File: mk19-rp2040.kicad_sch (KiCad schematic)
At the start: 134 parts, among them J1 USB_C_Receptacle_USB2.0, J10 Conn_01x02, J11 Conn_01x03_Socket, J12 USB_C_Receptacle_USB2.0, J13 USB_C_Receptacle_USB2.0, J2 Conn_01x03_Socket, J3 Conn_01x02_Socket, J4 Conn_01x06_Socket, J5 Conn_01x02, J7 Conn_01x02_Socket, J8 Conn_01x02_Socket, J9 Conn_01x02_Socket, T1 Conn_01x01_Socket, T10 Conn_01x01_Socket, T11 Conn_01x01_Socket, T12 Conn_01x01_Socket, T13 Conn_01x01_Socket, T14 Conn_01x01_Socket, T15 Conn_01x01_Socket, T2 Conn_01x01_Socket, T3 Conn_01x01_Socket, T5 Conn_01x01_Socket, T6 Conn_01x01_Socket, T7 Conn_01x01_Socket, T9 Conn_01x01_Socket, U1 RP2040, U10 1N4148W_C81598, U11 1N4148W_C81598, U12 1N4148W_C81598, U13 1N4148W_C81598, U14 1N4148W_C81598, U15 1N4148W_C81598, U2 USBLC6-2P6, U3 XC6210B332MR-G, U4 USBLC6-2P6, U5 W25Q128JVS, U6 8_01A0_008200, U7 8_01A0_008200, U8 USBLC6-2P6, U9 1N4148W_C81598, Y1 Crystal_GND24

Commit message: more changes, pcba insights coming next
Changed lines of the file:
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@@
-		)
-	)
-	(text_box "todo: Burkfers suggests 5v over serial is incorrect.\nreview how chunky does it."
-		(exclude_from_sim no)
-		(at 582.93 289.56 0)
-		(size 40.64 8.89)
-		(stroke
-			(width 0)
-			(type default)
-		)
-		(fill
-			(type none)
-		)
-		(effects
-			(font
-				(face "Futura")
-				(size 1.27 1.27)
-			)
-			(justify left top)
 		)
 	)

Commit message: reworking some of this, copy paste introduced errors whee
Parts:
- removed C20, C21, C22: CL31B105KBHNNNE, ct-kicad:C1206, symbol ct-kicad:CL31B105KBHNNNE
- removed U5: W25Q128JVS, drawings:W25Q128JVPIQ, symbol Memory_Flash:W25Q128JVS
- added C2, C28, C29: 10u, ct-kicad:C0805, symbol Device:C
- added FID1, FID2, FID3, FID4: Fiducial, Fiducial:Fiducial_1mm_Mask2mm, symbol Mechanical:Fiducial
- added U16: W25Q128JVSIQTR, ct-kicad:SOIC-8_L5.3-W5.3-P1.27-LS8.0-BL, symbol ct-kicad:W25Q128JVSIQTR
- C1, C27: footprint Capacitor_SMD:C_0805_2012Metric -> ct-kicad:C0805
- C10, C11, C12, C13, C14, C7, C8, C9: value 100n -> 100nf; footprint Capacitor_SMD:C_0402_1005Metric -> ct-kicad:C0402
- C15, C16: value CL31B105KBHNNNE -> 1u; footprint ct-kicad:C1206 -> ct-kicad:C0402; LCSC C1848 -> C52923
- C17, C5, C6: value 1µ -> 1u; footprint Capacitor_SMD:C_0402_1005Metric -> ct-kicad:C0402
- C18, C19, C23, C24, C25, C26: value 100nF -> 100nf
- C3, C4: footprint Capacitor_SMD:C_0402_1005Metric -> ct-kicad:C0402
- J11, J2, J4: now left out of the parts list
- R1, R10, R11, R12, R2, R20, R3, R4, R5, R6, R7, R8, R9: footprint Resistor_SMD:R_0402_1005Metric -> ct-kicad:R0402
- R13, R14: value 4.7k -> 5.1k; footprint ct-kicad:R1206 -> ct-kicad:R0402; LCSC C17902 -> C25905
- R15: value 1206W4F1002T5E -> 10k; footprint ct-kicad:R1206 -> ct-kicad:R0402; LCSC C17902 -> C25744
- U1: footprint 0xLib_Package_DFN_QFN:QFN-56-1EP_7x7mm_P0.4mm_EP3.2x3.2mm -> ct-kicad:LQFN-56_L7.0-W7.0-P0.4-EP
- U2, U4, U8: footprint Package_TO_SOT_SMD:SOT-666 -> ct-kicad:SOT-666-6_L1.6-W1.2-P0.50-LS1.6-BL
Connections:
- net +3V3: now also R13.2, R14.2, U16.8 (VCC)
- net +5V: no longer R13.2, R14.2
- net GND: now also C2.2, C28.2, C29.2, U16.4 (GND)
- net LED_5V: now also C2.1, C28.1, C29.1
- net QSPI_D0: now also U16.2 (DO)
- net QSPI_D1: now also U16.5 (DI)
- net QSPI_D2: now also U16.3 (IO2)
- net QSPI_D3: now also U16.7 (IO3)
- net QSPI_SCLK: now also U16.6 (CLK)
- net QSPI_~{CS}: now also U16.1 (CS#)
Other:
- note added: "Fiducials"

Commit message: drc passing, bom generating correctly, silkscreen v1
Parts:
- removed C1, C2, C27, C28, C29: 10u, ct-kicad:C0805, symbol Device:C
- removed PWR-OUT3: Conn_01x03_Socket, Connector_PinHeader_2.54mm:PinHeader_1x03_P2.54mm_Vertical, symbol Connector:Conn_01x03_Socket
- removed U2, U4, U8: USBLC6-2P6, ct-kicad:SOT-666-6_L1.6-W1.2-P0.50-LS1.6-BL, symbol Power_Protection:USBLC6-2P6
- added C1, C2, C27, C28, C29: 10u, ct-kicad:C0805, symbol ct-kicad:GRM21BR61H106KE43L
- added D5, D6, D7: USBLC6-2P6_C2827693, ct-kicad:SOT-666-6_L1.6-W1.2-P0.50-LS1.6-BL, symbol ct-kicad:USBLC6-2P6_C2827693
- added FB4, FB5, FB6: FerriteBead_Small, Inductor_SMD:L_0603_1608Metric, symbol Device:FerriteBead_Small
- added JP4: SolderJumper_3_Open, Jumper:SolderJumper-3_P1.3mm_Open_Pad1.0x1.5mm, symbol Jumper:SolderJumper_3_Open
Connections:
- net +3V3: now also C27.2
- net +5V: now also C1.2, D5.5 (VBUS), D6.5 (VBUS), D7.5 (VBUS), JP4.3 (B)
- net GND: now also C1.1, C2.1, C27.1, C28.1, C29.1, D5.2 (GND), D6.2 (GND), D7.2 (GND), FB4.1, FB5.1, FB6.1
- net LED_5V: now also C2.2, C28.2, C29.2
- net LED_SCREEN_DI: now also D6.3 (I/O2), D6.4 (I/O2)
- net LED_SCREEN_DO: now also D6.1 (I/O1), D6.6 (I/O1)
- net Serial-RX: now also D5.1 (I/O1), D5.6 (I/O1)
- net Serial-TX: now also D5.3 (I/O2), D5.4 (I/O2)
- net USB-MAIN_+: now also D7.3 (I/O2), D7.4 (I/O2)
- net USB-MAIN_-: now also D7.1 (I/O1), D7.6 (I/O1)
- net at FB3.2, J13.S (SHIELD): now also FB6.2
- net at JP1.2 (C): now also JP4.2 (C)
- net at FB2.2, J12.S (SHIELD): now also FB5.2
- net at PWR-EXT-IN1.2 (Pin_2): now also JP4.1 (A)
- net at FB1.2, J1.S (SHIELD): now also FB4.2

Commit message: getting manufacturing bits ready
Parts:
- added H5, H6, H7, H8: MountingHole, MountingHole:MountingHole_2.1mm, symbol Mechanical:MountingHole
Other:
- note added: "Fiducials and tooling holes"
- note removed: "Fiducials"
- moved on the sheet: FID1, FID2, FID3, FID4

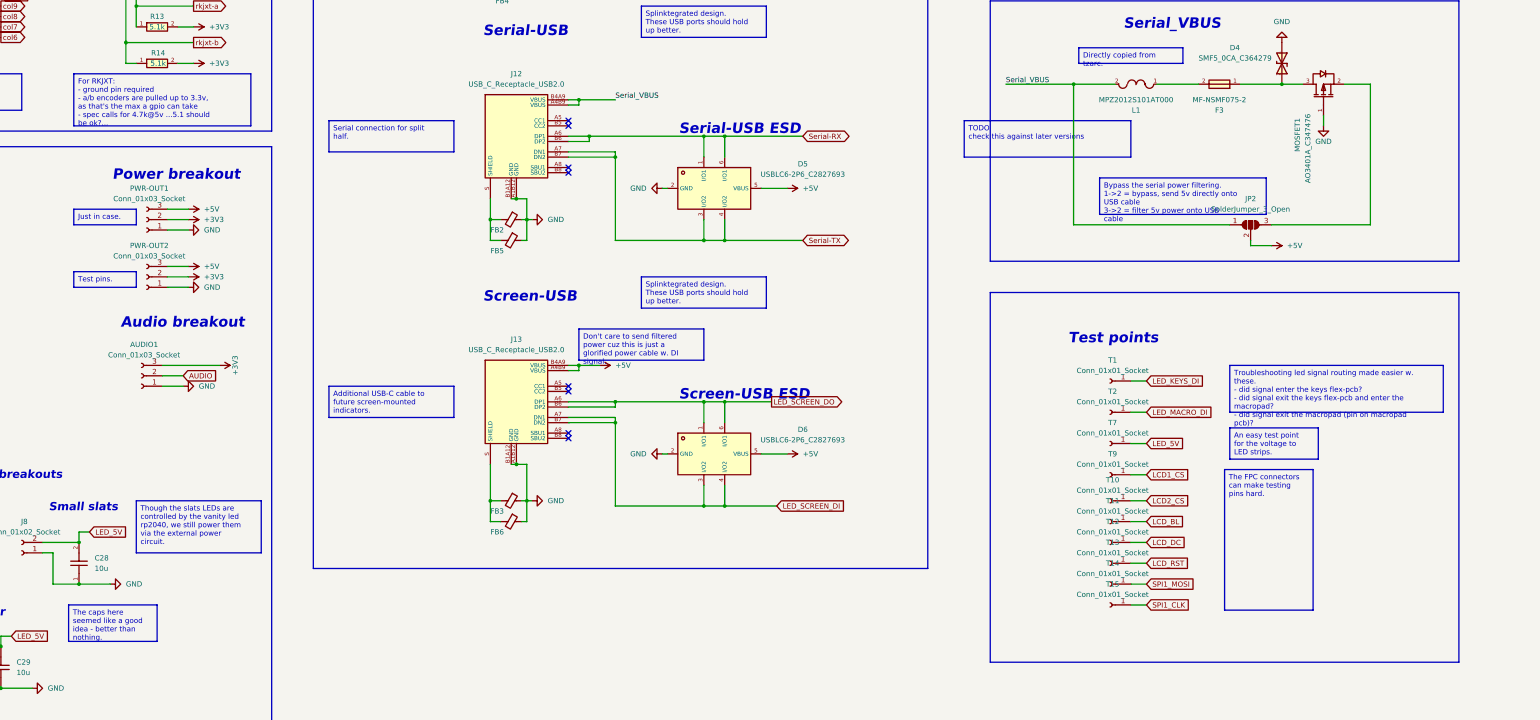
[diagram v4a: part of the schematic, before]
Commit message: moving away from through-hole test points
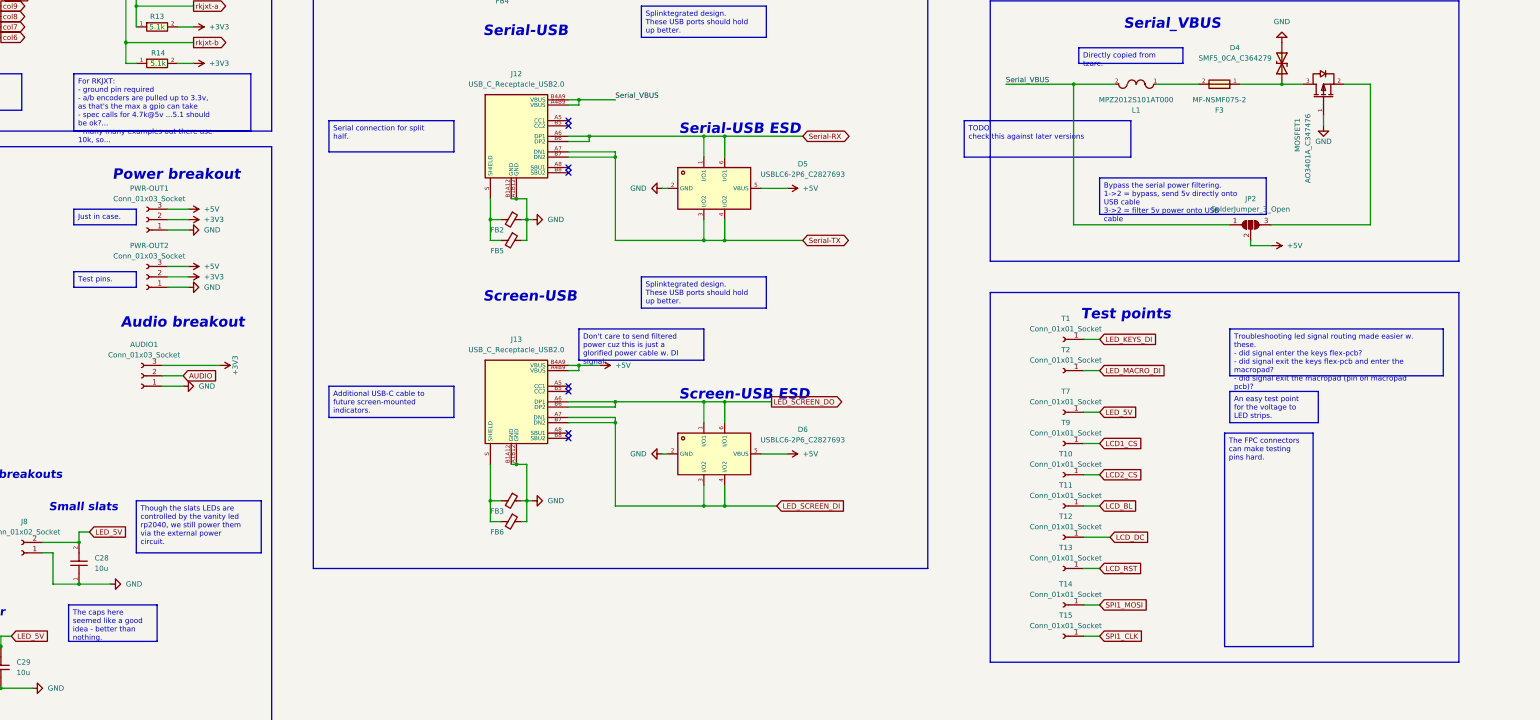
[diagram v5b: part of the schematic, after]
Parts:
- T1, T10, T11, T12, T13, T14, T15, T2, T9: footprint Connector_Pin:Pin_D1.0mm_L10.0mm -> TestPoint:TestPoint_Pad_1.0x1.0mm
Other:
- moved on the sheet: T1, T10, T11, T12, T13, T14, T15, T2, T7, T9

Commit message: relocating boot debug reset to edges of board, edge rail improvements
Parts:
- FID1, FID2, FID3, FID4: footprint Fiducial:Fiducial_1mm_Mask2mm -> Fiducial:Fiducial_1mm_Mask3mm
- H5, H6, H7, H8: footprint MountingHole:MountingHole_2.1mm -> ct-kicad:hole-tooling-2mm
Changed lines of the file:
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@@
 			)
 		)
-		(property "Footprint" "Fiducial:Fiducial_1mm_Mask2mm"
+		(property "Footprint" "Fiducial:Fiducial_1mm_Mask3mm"
 			(at 60.96 415.29 0)
 			(effects
@@
 			)
 		)
-		(property "Footprint" "MountingHole:MountingHole_2.1mm"
+		(property "Footprint" "ct-kicad:hole-tooling-2mm"
 			(at 43.18 421.64 0)
 			(effects
@@
 			)
 		)
-		(property "Footprint" "MountingHole:MountingHole_2.1mm"
+		(property "Footprint" "ct-kicad:hole-tooling-2mm"
 			(at 43.18 427.99 0)
 			(effects
@@
 			)
 		)
-		(property "Footprint" "Fiducial:Fiducial_1mm_Mask2mm"
+		(property "Footprint" "Fiducial:Fiducial_1mm_Mask3mm"
 			(at 43.18 415.29 0)
 			(effects
@@
 			)
 		)
-		(property "Footprint" "MountingHole:MountingHole_2.1mm"
+		(property "Footprint" "ct-kicad:hole-tooling-2mm"
 			(at 60.96 427.99 0)
 			(effects
@@
 			)
 		)
-		(property "Footprint" "MountingHole:MountingHole_2.1mm"
+		(property "Footprint" "ct-kicad:hole-tooling-2mm"
 			(at 60.96 421.64 0)
 			(effects
@@
 			)
 		)
-		(property "Footprint" "Fiducial:Fiducial_1mm_Mask2mm"
+		(property "Footprint" "Fiducial:Fiducial_1mm_Mask3mm"
 			(at 43.18 408.94 0)
 			(effects
@@
 			)
 		)
-		(property "Footprint" "Fiducial:Fiducial_1mm_Mask2mm"
+		(property "Footprint" "Fiducial:Fiducial_1mm_Mask3mm"
 			(at 60.96 408.94 0)
 			(effects

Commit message: just about ready to produce
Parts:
- removed LOGO3: **REF, ct-kicad:mk19-qr-logo-12mm, symbol ct-kicad:mk19-qr-12mm
- added LOGO8: **REF, ct-kicad:qr-mk19-rp2040-10mm, symbol ct-kicad:mk19-rp2040-qr-10mm
- J10, J5: footprint Connector_PinSocket_2.54mm:PinSocket_1x02_P2.54mm_Vertical -> Connector_JST:JST_XH_B2B-XH-A_1x02_P2.50mm_Vertical
- J11: footprint Connector_JST:JST_XH_B3B-XH-A_1x03_P2.50mm_Vertical -> Connector_JST:JST_XH_S3B-XH-A_1x03_P2.50mm_Horizontal
- J7, J8, J9, PWR-EXT-IN1: footprint Connector_JST:JST_XH_B2B-XH-A_1x02_P2.50mm_Vertical -> Connector_JST:JST_XH_S2B-XH-A_1x02_P2.50mm_Horizontal
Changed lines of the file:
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@@
 			)
 		)
-		(property "Footprint" "Connector_PinSocket_2.54mm:PinSocket_1x02_P2.54mm_Vertical"
+		(property "Footprint" "Connector_JST:JST_XH_B2B-XH-A_1x02_P2.50mm_Vertical"
 			(at 354.33 189.23 0)
 			(effects
@@
 	)
 	(symbol
-		(lib_id "ct-kicad:mk19-qr-12mm")
-		(at 48.26 377.19 0)
-		(unit 1)
-		(exclude_from_sim no)
-		(in_bom no)
-		(on_board yes)
-		(dnp no)
-		(fields_autoplaced yes)
-		(property "Reference" "LOGO3"
-			(at 50.8 375.92 0)
-			(effects
-				(font
-					(size 1.27 1.27)
-				)
-				(justify left)
-			)
-		)
-		(property "Value" "**REF"
-			(at 50.8 378.46 0)
-			(effects
-				(font
-					(size 1.27 1.27)
-				)
-				(justify left)
-			)
-		)
-		(property "Footprint" "ct-kicad:mk19-qr-logo-12mm"
-			(at 48.26 377.19 0)
-			(effects
-				(font
-					(size 1.27 1.27)
-				)
-				(hide yes)
-			)
-		)
-		(property "Datasheet" ""
-			(at 48.26 377.19 0)
-			(effects
-				(font
-					(size 1.27 1.27)
-				)
-				(hide yes)
-			)
-		)
-		(property "Description" ""
-			(at 48.26 377.19 0)
-			(effects
-				(font
-					(size 1.27 1.27)
-				)
-				(hide yes)
-			)
-		)
-		(instances
-			(project "mk19-rp2040"
-				(path "/7353e96a-343a-4876-b497-b1d205a14d97"
-					(reference "LOGO3")
-					(unit 1)
-				)
-			)
-		)
-	)
-	(symbol
 		(lib_id "Jumper:SolderJumper_3_Open")
 		(at 152.4 408.94 0)
@@
 			)
 		)
-		(property "Footprint" "Connector_JST:JST_XH_B2B-XH-A_1x02_P2.50mm_Vertical"
+		(property "Footprint" "Connector_JST:JST_XH_S2B-XH-A_1x02_P2.50mm_Horizontal"
 			(at 229.87 429.26 0)
 			(effects
@@
 			)
 		)
-		(property "Footprint" "Connector_PinSocket_2.54mm:PinSocket_1x02_P2.54mm_Vertical"
+		(property "Footprint" "Connector_JST:JST_XH_B2B-XH-A_1x02_P2.50mm_Vertical"
 			(at 410.21 123.19 0)
 			(effects
@@
 			)
 		)
-		(property "Footprint" "Connector_JST:JST_XH_B2B-XH-A_1x02_P2.50mm_Vertical"
+		(property "Footprint" "Connector_JST:JST_XH_S2B-XH-A_1x02_P2.50mm_Horizontal"
 			(at 134.62 411.48 0)
 			(effects
@@
 			)
 		)
-		(property "Footprint" "Connector_JST:JST_XH_B2B-XH-A_1x02_P2.50mm_Vertical"
+		(property "Footprint" "Connector_JST:JST_XH_S2B-XH-A_1x02_P2.50mm_Horizontal"
 			(at 209.55 403.86 0)
 			(effects
@@
 			)
 		)
-		(property "Footprint" "Connector_JST:JST_XH_B3B-XH-A_1x03_P2.50mm_Vertical"
+		(property "Footprint" "Connector_JST:JST_XH_S3B-XH-A_1x03_P2.50mm_Horizontal"
 			(at 405.13 147.32 0)
 			(effects
@@
 	)
 	(symbol
+		(lib_id "ct-kicad:mk19-rp2040-qr-10mm")
+		(at 48.26 383.54 0)
+		(unit 1)
+		(exclude_from_sim no)
+		(in_bom no)
+		(on_board yes)
+		(dnp no)
+		(fields_autoplaced yes)
+		(property "Reference" "LOGO8"
+			(at 48.26 383.54 0)
+			(effects
+				(font
+					(size 1.27 1.27)
+				)
+				(hide yes)
+			)
+		)
+		(property "Value" "**REF"
+			(at 48.26 383.54 0)
+			(effects
+				(font
+					(size 1.27 1.27)
+				)
+				(hide yes)
+			)
+		)
+		(property "Footprint" "ct-kicad:qr-mk19-rp2040-10mm"
+			(at 48.26 383.54 0)
+			(effects
+				(font
+					(size 1.27 1.27)
+				)
+				(hide yes)
+			)
+		)
+		(property "Datasheet" ""
+			(at 48.26 383.54 0)
+			(effects
+				(font
+					(size 1.27 1.27)
+				)
+				(hide yes)
+			)
+		)
+		(property "Description" "qr code for repo"
+			(at 48.26 383.54 0)
+			(effects
+				(font
+					(size 1.27 1.27)
+				)
+				(hide yes)
+			)
+		)
+		(instances
+			(project "mk19-rp2040"
+				(path "/7353e96a-343a-4876-b497-b1d205a14d97"
+					(reference "LOGO8")
+					(unit 1)
+				)
+			)
+		)
+	)
+	(symbol
 		(lib_id "ct-kicad:74HC595D,118")
 		(at 151.13 69.85 0)
@@
 			)
 		)
-		(property "Footprint" "Connector_JST:JST_XH_B2B-XH-A_1x02_P2.50mm_Vertical"
+		(property "Footprint" "Connector_JST:JST_XH_S2B-XH-A_1x02_P2.50mm_Horizontal"
 			(at 248.92 403.86 0)
 			(effects
